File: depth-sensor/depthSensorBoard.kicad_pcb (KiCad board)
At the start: 2 copper layers, 58.4 x 47 mm, 33 parts, among them IC1 ATMEGA1284P-M, M1 MountingHole_3.5mm, M2 MountingHole_3.5mm, M3 MountingHole_3.5mm, M4 MountingHole_3.5mm, M5 MountingHole_3.5mm, M6 MountingHole_3.5mm, M8 MountingHole_3.5mm, P1 Mezzanine-Header, P2 CONN_02X03, P3 CONN_01X04, P4 CONN_01X04, P5 CONN_01X04, P6 CONN_01X04, Q2 Q_NJFET_GSD, U1 AP2112, U2 TCA9545A, U3 TSX-3225

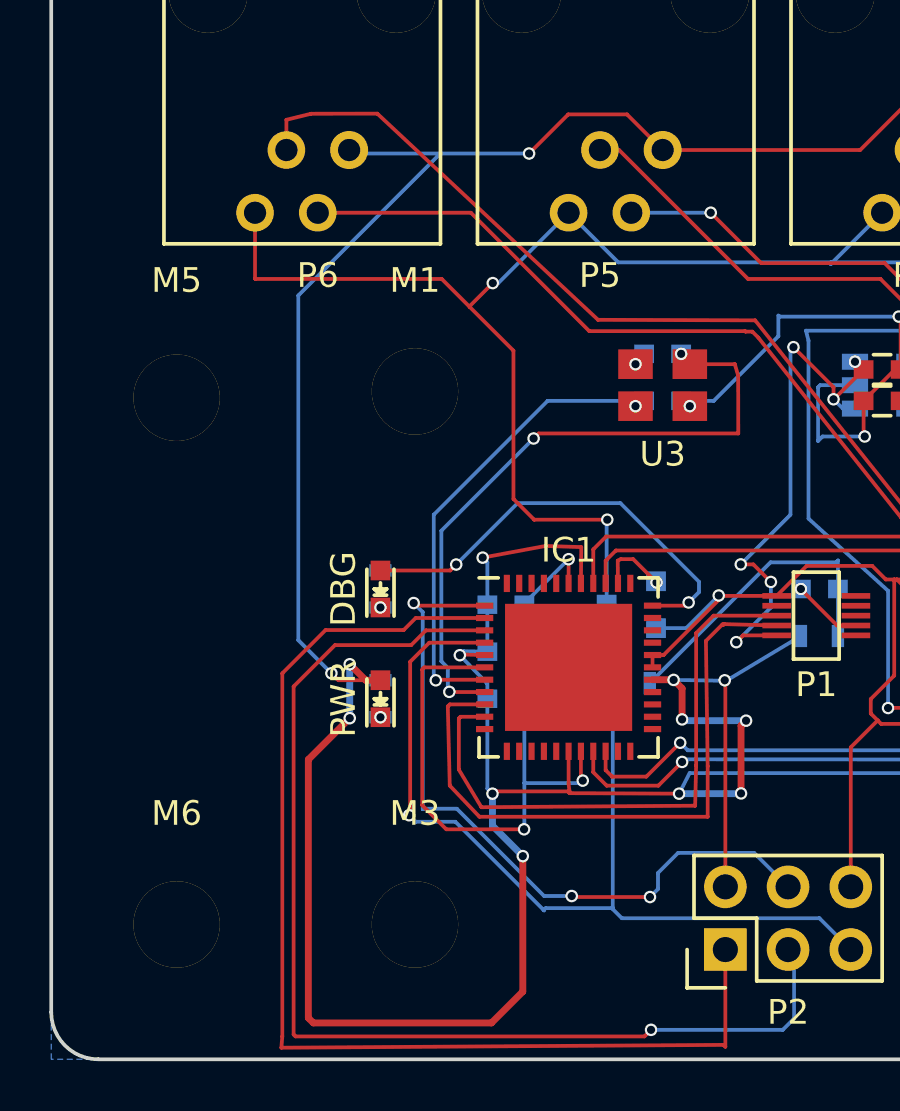
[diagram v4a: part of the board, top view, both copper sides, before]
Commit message: Redid some connections
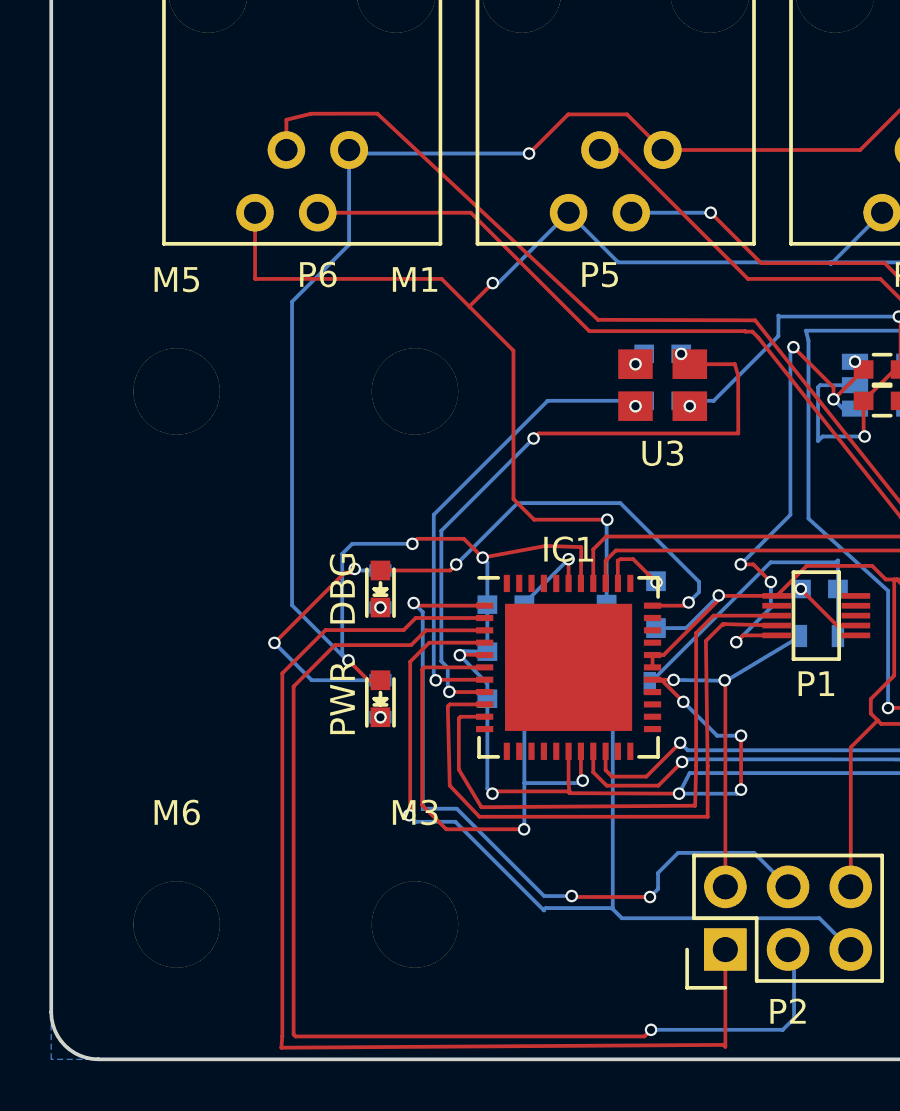
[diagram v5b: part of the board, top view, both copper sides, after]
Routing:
- net +3V3: track 202.6 -> 176.5 mm, vias 18 -> 16
- net GND: track 88.3 -> 98.8 mm, vias 8 -> 10
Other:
- net class PWR removed

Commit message: Routing completed(if nothing is seen as incorrect)
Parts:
- moved C6 4.89 mm to (119.0, 132.5), turned to 90 degrees
- moved Q2 4.78 mm to (119.0, 127.4), turned to 0 degrees
- moved C8 4.25 mm to (122.9, 132.5), turned to 90 degrees
- moved C7 3.70 mm to (121.0, 132.5), turned to 90 degrees
- moved R2 3.63 mm to (124.8, 127.3), turned to 90 degrees
- moved U2 1.55 mm to (141.9, 129.6), turned to 180 degrees
- moved P2 0.43 mm to (127.9, 141.3)
- moved IC1 0.37 mm to (121.6, 130.0), turned to 90 degrees
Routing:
- net /ATMega1284p/MISO: track 46.2 -> 13.8 mm
- net /ATMega1284p/SCK: track 46.3 -> 15.6 mm, vias 2 -> 0
- net +3V3: track 176.5 -> 146.3 mm, vias 16 -> 8
- net /ATMega1284p/~RST: track 38.9 -> 64.9 mm, vias 2 -> 6
- net /SCL2: track 49.0 -> 24.3 mm, vias 4 -> 0
- net GND: track 98.8 -> 123.2 mm, vias 10 -> 11
- net /SDA2: track 50.3 -> 27.1 mm
- net /SDA3: track 59.7 -> 38.3 mm, vias 0 -> 4
- net /SCL: track 35.2 -> 15.6 mm, vias 2 -> 0
- net /~RST: track 18.1 -> 37.5 mm
- net Net-(C5-Pad1): track 19.6 -> 37.8 mm, vias 2 -> 4
- net /SCL3: track 53.9 -> 36.2 mm, vias 0 -> 2
- net Net-(C2-Pad1): track 27.0 -> 43.8 mm, vias 3 -> 6
- net /SDA: track 32.5 -> 15.9 mm
- net /ATMega1284p/MOSI: track 29.6 -> 16.1 mm, vias 4 -> 2
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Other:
- net class PWR added: clearance 0.1524, trace_width 0.2788, via_dia 0.508, via_drill 0.3302

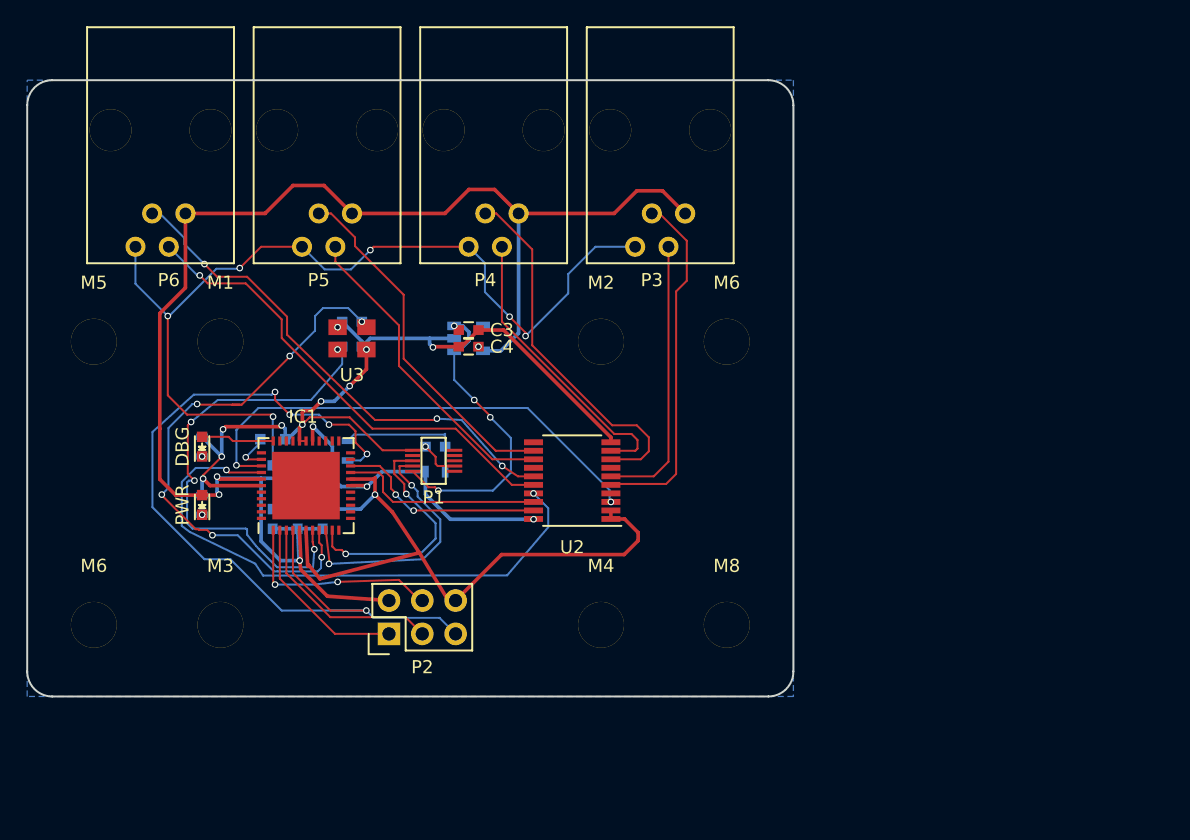
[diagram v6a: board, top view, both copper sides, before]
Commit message: Removed extra mounting holes, added logo, moved header pins
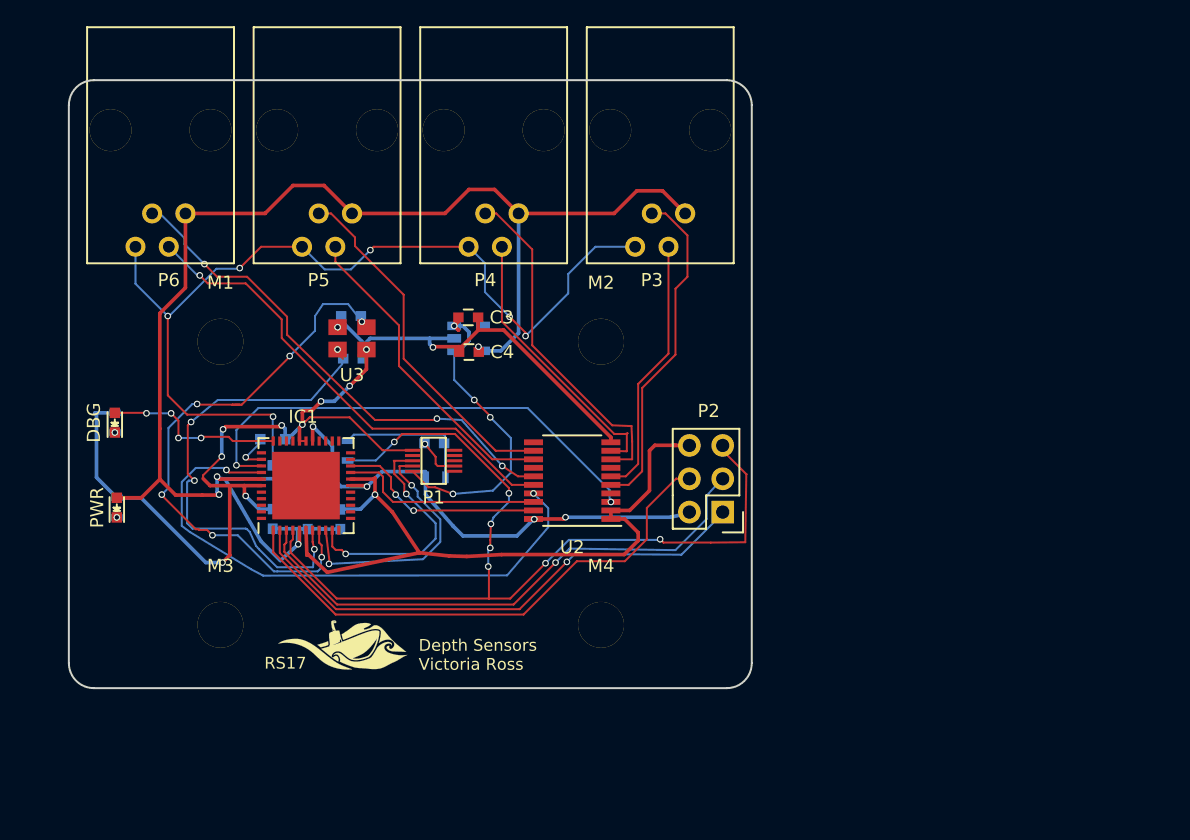
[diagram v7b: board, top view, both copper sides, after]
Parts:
- removed M5, M6 (x2), M8: MountingHole_3.5mm, Mounting_Holes:MountingHole_3.5mm
- added G***: LOGO, robosub_footprints:robosub_logo-medium, F.Cu at (124.5, 142.2)
- moved P2 27.1 mm to (153.4, 132.0), turned to 180 degrees
- moved DBG 6.90 mm to (107.0, 125.2)
- moved R6 6.90 mm to (107.0, 125.2)
- moved PWR 6.51 mm to (107.2, 131.6)
- moved R5 6.51 mm to (107.2, 131.6)
- moved C8 1.35 mm to (124.2, 132.5)
- moved C3 0.97 mm to (134.0, 117.1)
- moved C5 0.92 mm to (125.2, 120.3)
- moved C7 0.76 mm to (121.7, 132.5)
- moved C2 0.44 mm to (125.0, 117.0)
- moved R1 0.43 mm to (131.5, 129.3)
- moved C4 0.41 mm to (134.0, 119.8)
- moved C1 0.27 mm to (131.4, 126.7)
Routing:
- net GND: track 123.2 -> 159.5 mm, vias 11 -> 12
- net /ATMega1284p/MISO: track 13.8 -> 40.4 mm, vias 0 -> 2
- net /ATMega1284p/SCK: track 15.6 -> 41.8 mm, vias 0 -> 2
- net /ATMega1284p/MOSI: track 16.1 -> 41.1 mm, vias 2 -> 0
- net +3V3: track 146.3 -> 156.3 mm, vias 8 -> 10
- net /DBG_LED: track 5.56 -> 13.7 mm, vias 0 -> 4
- net /ATMega1284p/~RST: track 64.9 -> 71.9 mm, vias 6 -> 7
- net /SDA1: track 28.0 -> 26.3 mm
- net /SCL0: track 21.2 -> 20.0 mm
- net Net-(C5-Pad1): track 37.8 -> 38.9 mm
- net /SCL1: track 22.5 -> 21.4 mm
- net Net-(C2-Pad1): track 43.8 -> 44.7 mm
- net +5V: track 23.7 -> 24.4 mm
- net /SDA0: track 27.0 -> 26.3 mm
- removed copper zone on B.Cu, net GND
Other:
- board size 58.4 x 47 mm -> 52.1 x 46.4 mm
- board text added: "Depth Sensors Victoria Ross"
- board text added: "RS17"

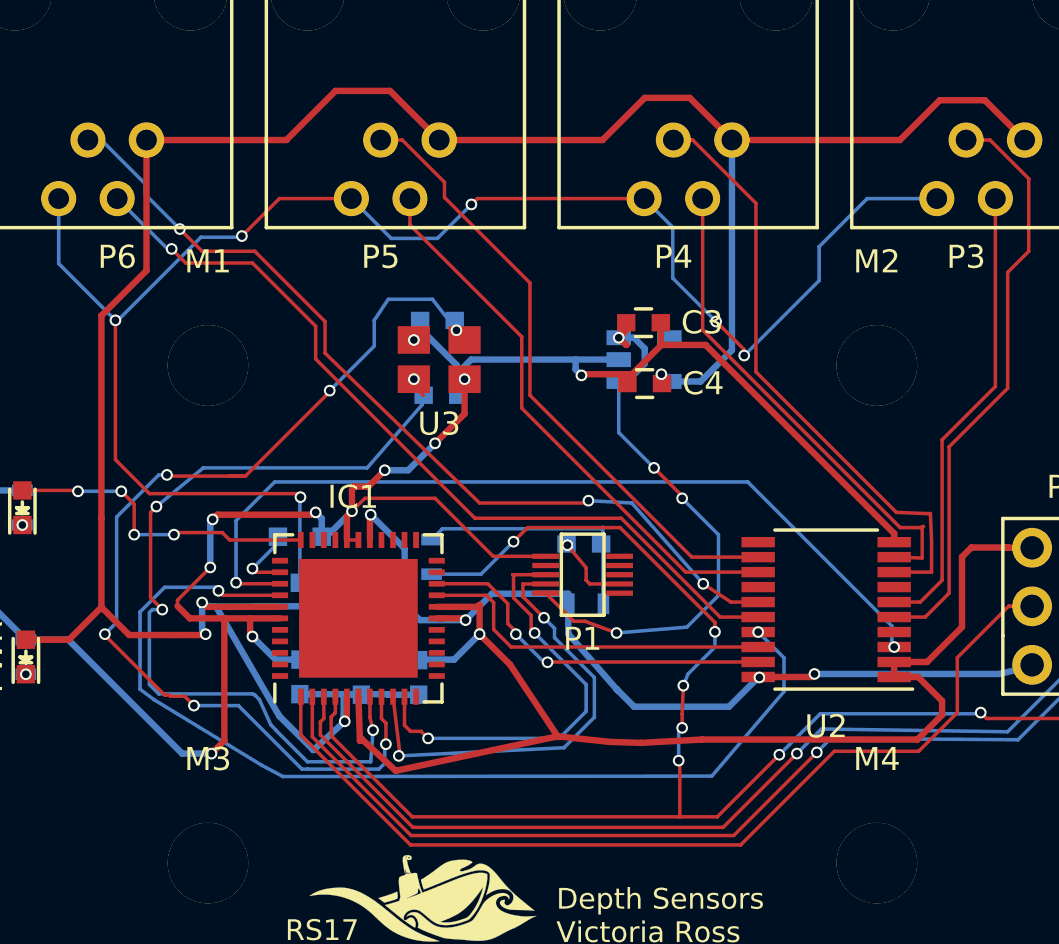
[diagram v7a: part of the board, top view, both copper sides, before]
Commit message: Added footprint of mezzanine header/fixed routing
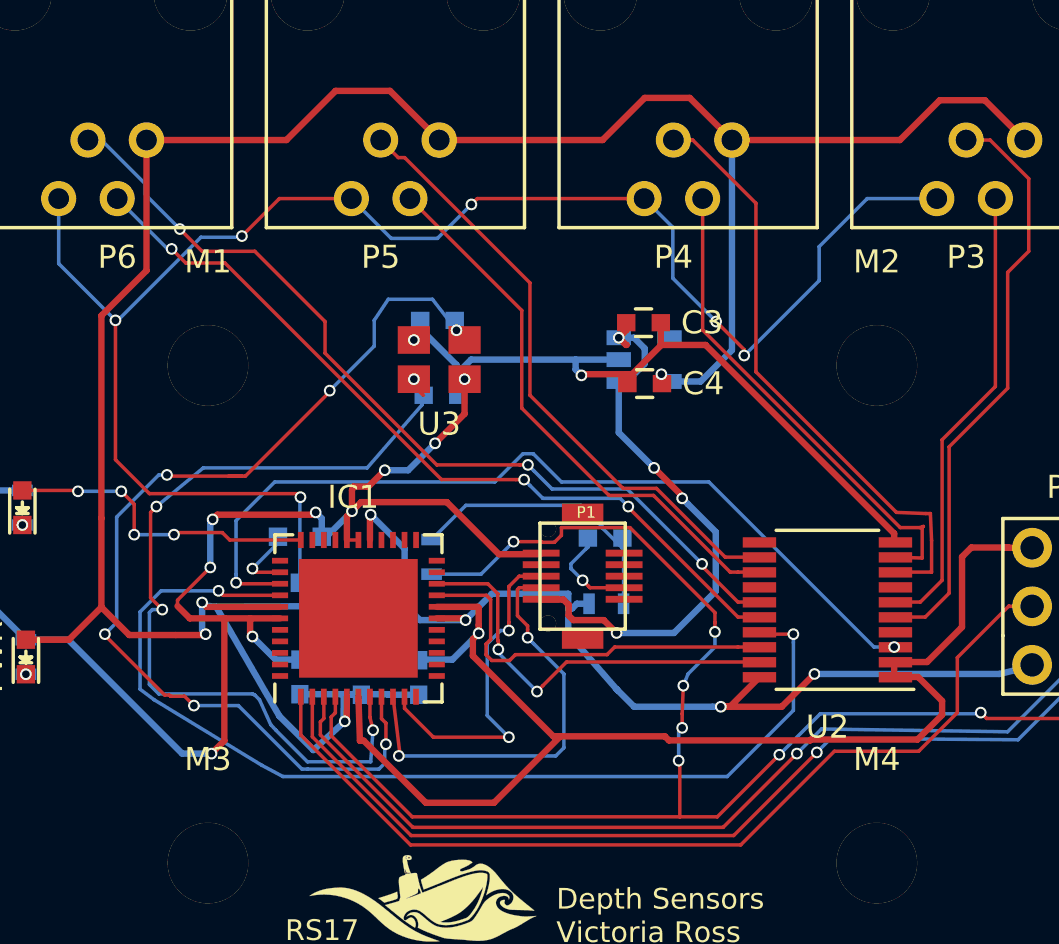
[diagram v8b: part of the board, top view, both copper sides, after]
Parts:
- P1: footprint robosub_footprints:DF40C-10DP-Header -> robosub_footprints:3mm-10pos-receptacle
- moved C1 0.96 mm to (132.3, 126.5)
- moved R1 0.88 mm to (132.3, 129.3)
- moved P1 0.06 mm to (131.3, 128.1)
- moved U2 0.06 mm to (141.9, 129.6)
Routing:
- net /Rx_CPU: track 18.5 -> 14.7 mm
- net +3V3: track 156.3 -> 159.4 mm
- net Net-(C1-Pad1): track 10.5 -> 12.7 mm
- net /SDA: track 15.9 -> 17.9 mm
- net GND: track 159.5 -> 161.4 mm
- net /~INT: track 43.8 -> 45.3 mm
- net /SCL: track 15.6 -> 17.0 mm
- net /DTR: track 3.34 -> 4.37 mm
- net /Tx_CPU: track 19.7 -> 18.7 mm
- net /SCL3: track 36.2 -> 35.4 mm, vias 2 -> 4
- net +5V: track 24.4 -> 25.2 mm
